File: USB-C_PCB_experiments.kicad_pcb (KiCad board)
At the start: 2 copper layers, 15 x 97 mm, 32 parts, among them J1 USB-C fingers, J10 FFC programming interface, J2 FFC programming interface, J3 Conn_01x08, J4 Conn_01x08, J5 USB-C fingers, J6 FFC programming interface, J9 USB-C fingers, U1 ATtiny84A-CC, U2 ATtiny84A-CC, U4 ATtiny84A-CC

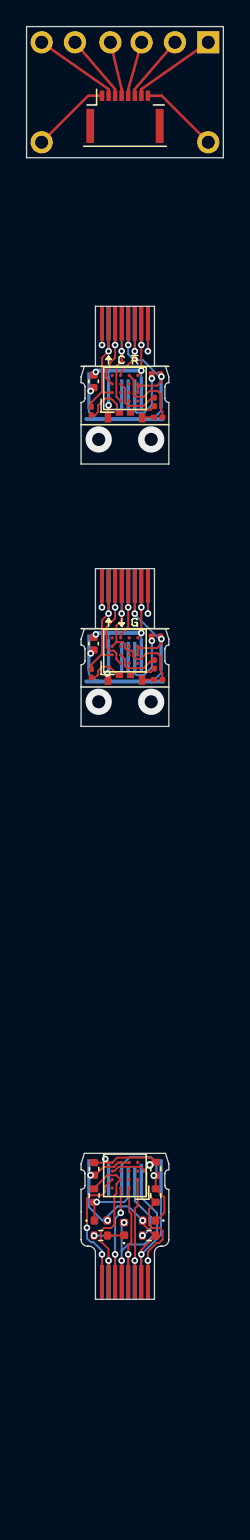
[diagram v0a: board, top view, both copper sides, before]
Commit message: Finished routing Demo 2, added Demo 4, updated readme with newer findings
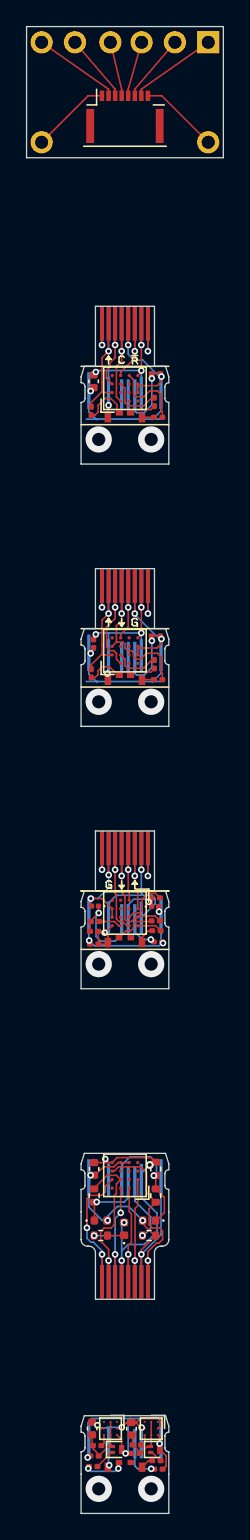
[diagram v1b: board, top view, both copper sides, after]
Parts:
- added C3: 0.1μF, Capacitor_SMD:C_0201_0603Metric, F.Cu at (97.7, 102.4)
- added C5: 10μF, Capacitor_SMD:C_0402_1005Metric, F.Cu at (97.5, 139.3)
- added C6: 10μF, Capacitor_SMD:C_0402_1005Metric, F.Cu at (100.5, 139.3)
- added C7: 2.2μF, Capacitor_SMD:C_0201_0603Metric, F.Cu at (97.7, 141.4)
- added C8: 2.2μF, Capacitor_SMD:C_0201_0603Metric, F.Cu at (100.8, 141.2)
- added D5: 3.6V, awful-usb-socket:D_X3DFN2, F.Cu at (97.7, 99.5)
- added D6: 3.6V, awful-usb-socket:D_X3DFN2, F.Cu at (102.3, 99.5)
- added D7: LED_AGRB, USB-C_PCB_experiments:LED_everlight_EASV2713RGBA1, F.Cu at (100.0, 102.2)
- added D9: LED_AGRB, USB-C_PCB_experiments:LED_everlight_EASV2713RGBA1, F.Cu at (100.0, 142.2)
- added J11: USB-C fingers, awful-usb-socket:usb-c-one-sided, B.Cu at (100.0, 140.6)
- added J7: USB-C fingers, awful-usb-socket:usb-c-one-sided, B.Cu at (100.0, 100.5)
- added J8: FFC programming interface, USB-C_PCB_experiments:FFC-08, F.Cu at (100.0, 95.0)
- added Q1: PMBT3906M, Package_TO_SOT_SMD:SOT-883, F.Cu at (99.4, 140.9)
- added Q2: PMBT3906M, Package_TO_SOT_SMD:SOT-883, F.Cu at (102.3, 140.9)
- added R10: 10kΩ, Resistor_SMD:R_0201_0603Metric, F.Cu at (102.5, 102.2)
- added R11: 1.5kΩ, Resistor_SMD:R_0201_0603Metric, F.Cu at (97.7, 101.4)
- added R12: 68Ω, Resistor_SMD:R_0201_0603Metric, F.Cu at (97.7, 100.7)
- added R13: 68Ω, Resistor_SMD:R_0201_0603Metric, F.Cu at (102.3, 98.8)
- added R19: 220, Resistor_SMD:R_0201_0603Metric, F.Cu at (102.3, 100.6)
- added R20: 220, Resistor_SMD:R_0201_0603Metric, F.Cu at (102.4, 101.3)
- added R21: 10k, Resistor_SMD:R_0201_0603Metric, F.Cu at (102.5, 142.4)
- added R22: 100kΩ, Resistor_SMD:R_0201_0603Metric, F.Cu at (97.9, 140.6)
- added R23: 120kΩ, Resistor_SMD:R_0201_0603Metric, F.Cu at (100.9, 140.6)
- added R24: 220, Resistor_SMD:R_0201_0603Metric, F.Cu at (97.6, 142.2)
- added R25: 220, Resistor_SMD:R_0201_0603Metric, F.Cu at (102.4, 141.8)
- added U3: ATtiny84A-CC, Package_BGA:UFBGA-15_3.0x3.0mm_Layout4x4_P0.65mm, F.Cu at (100.0, 100.0)
- added U5: LMC555xTP, Package_BGA:Texas_DSBGA-8_1.43x1.41mm_Layout3x3_P0.5mm, F.Cu at (98.9, 139.3)
- added U6: LMC555xTP, Package_BGA:Texas_DSBGA-8_1.43x1.41mm_Layout3x3_P0.5mm, F.Cu at (102.0, 139.3)
- C4: footprint Capacitor_SMD:C_0402_1005Metric -> Capacitor_SMD:C_0201_0603Metric
- R6: value 68Ω -> 1.5kΩ
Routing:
- net /RGB Dingus Programmable/GND: track 0.00 -> 20.7 mm, vias 0 -> 5
- net /555 RGB/GND: track 0.00 -> 18.6 mm, vias 0 -> 3
- net /RGB Dingus Programmable/V: track 0.00 -> 16.9 mm, vias 0 -> 2
- net /555 RGB/V: track 0.00 -> 12.1 mm, vias 0 -> 4
- net /RGB Dingus Programmable/MOSI: track 0.00 -> 10.7 mm, vias 0 -> 1
- net /RGB Dingus Programmable/~{RST}: track 0.00 -> 8.13 mm, vias 0 -> 1
- net /RGB Dingus Programmable/D-: track 0.00 -> 7.59 mm, vias 0 -> 1
- net /RGB Dingus Programmable/MISO: track 0.00 -> 6.84 mm, vias 0 -> 1
- net /RGB Dingus Programmable/SCK: track 0.00 -> 5.66 mm, vias 0 -> 1
- net /555 RGB/trg: track 0.00 -> 5.11 mm
- net /555 RGB/trb: track 0.00 -> 4.61 mm
- net unconnected-(J8-Pad8): track 0.00 -> 4.25 mm, vias 0 -> 1
- net /RGB Dingus Programmable/D+: track 0.00 -> 4.08 mm, vias 0 -> 1
- net /RGB Dingus Programmable/PB1: track 0.00 -> 3.77 mm
- net unconnected-(J8-Pad1): track 0.00 -> 3.30 mm, vias 0 -> 1
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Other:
- board size 15 x 97 mm -> 15 x 113.4 mm
- board text added: "GB LED USB-C dingus, BGA 555 ICs Flex PCB"
- board text added: "GB LED USB-C dingus, with bootloader Flex PCB"
- board text removed: "RGB LED USB-C dingus, with bootloader Flex PCB (Will be here soon)"
